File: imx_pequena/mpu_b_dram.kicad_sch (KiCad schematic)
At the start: 19 parts, among them U1 MCIMX6Z0DVM09AB, U2 MT41K64M16TW-107:J_TR

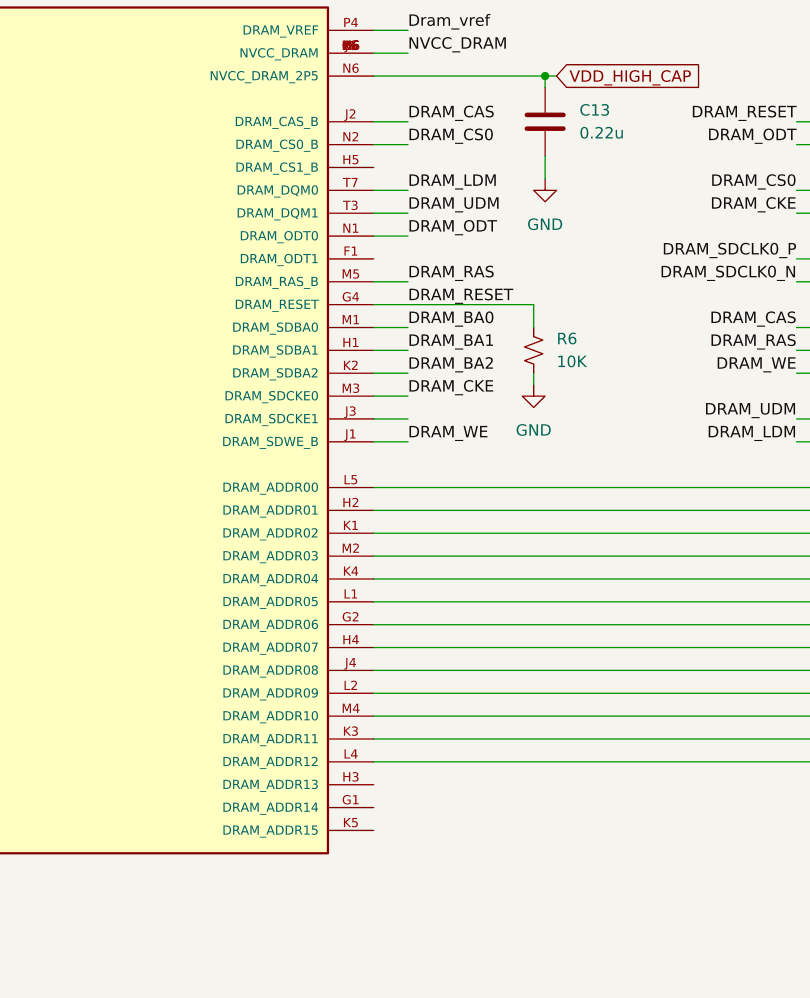
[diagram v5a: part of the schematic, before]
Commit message: Pinout updates
Updated pinout files, changed pinout of gpio 1 and 3
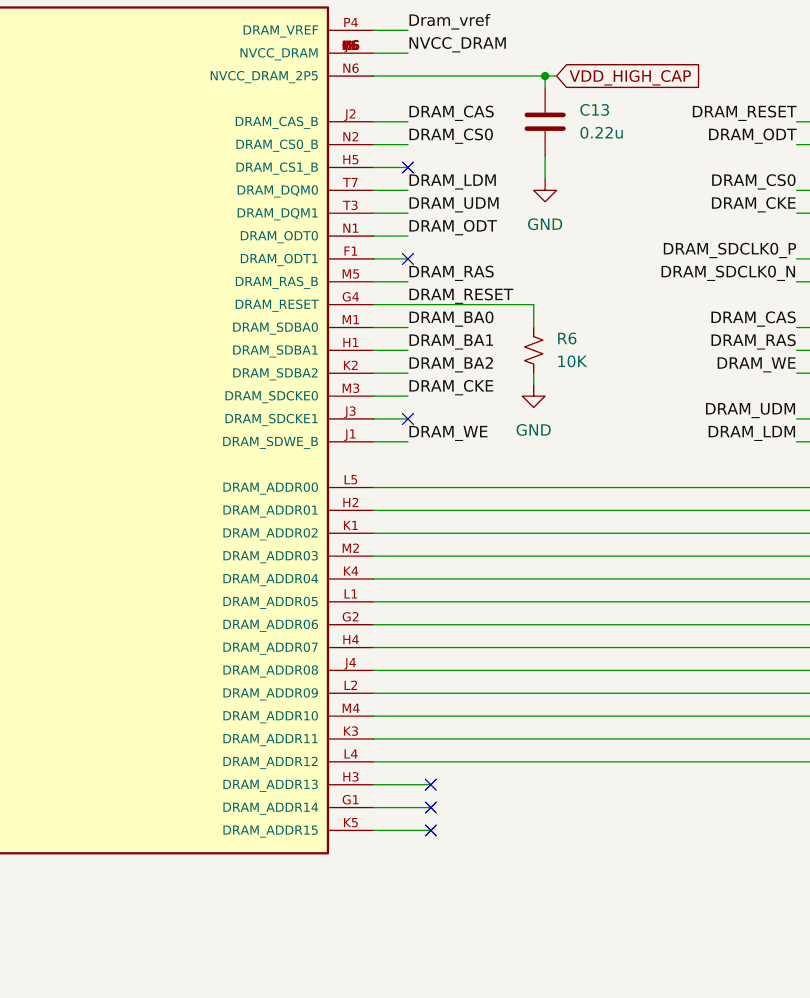
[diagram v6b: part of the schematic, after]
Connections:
- no-connect marks 0 -> 6
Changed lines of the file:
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@@
   (junction (at 76.2 181.61) (diameter 0) (color 0 0 0 0)
   )
+  (no_connect (at 124.46 63.5))
+  (no_connect (at 124.46 53.34))
+  (no_connect (at 124.46 81.28))
+  (no_connect (at 127 121.92))
+  (no_connect (at 127 124.46))
+  (no_connect (at 127 127))
   (bus_entry (at 255.27 88.9) (size -2.54 2.54)
     (stroke (width 0) (type default) (color 0 0 0 0))
@@
     (stroke (width 0) (type default) (color 0 0 0 0))
   )
+  (wire (pts (xy 120.65 63.5) (xy 124.46 63.5))
+    (stroke (width 0) (type default) (color 0 0 0 0))
+  )
   (wire (pts (xy 52.07 119.38) (xy 59.69 119.38))
     (stroke (width 0) (type default) (color 0 0 0 0))
@@
     (stroke (width 0) (type default) (color 0 0 0 0))
   )
+  (wire (pts (xy 120.65 121.92) (xy 127 121.92))
+    (stroke (width 0) (type default) (color 0 0 0 0))
+  )
   (wire (pts (xy 52.07 127) (xy 59.69 127))
     (stroke (width 0) (type default) (color 0 0 0 0))
@@
     (stroke (width 0) (type default) (color 0 0 0 0))
   )
+  (wire (pts (xy 120.65 124.46) (xy 127 124.46))
+    (stroke (width 0) (type default) (color 0 0 0 0))
+  )
   (wire (pts (xy 276.86 24.13) (xy 276.86 22.86))
     (stroke (width 0) (type default) (color 0 0 0 0))
@@
     (stroke (width 0) (type default) (color 0 0 0 0))
   )
+  (wire (pts (xy 120.65 53.34) (xy 124.46 53.34))
+    (stroke (width 0) (type default) (color 0 0 0 0))
+  )
   (wire (pts (xy 139.7 52.07) (xy 139.7 54.61))
     (stroke (width 0) (type default) (color 0 0 0 0))
@@
     (stroke (width 0) (type default) (color 0 0 0 0))
   )
+  (wire (pts (xy 120.65 127) (xy 127 127))
+    (stroke (width 0) (type default) (color 0 0 0 0))
+  )

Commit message: Part Assignment
Assigned GPIOs and assigned footprints to most parts
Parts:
- C10, C11, C12, C13, C14, C15, C16, C17, C8, C9: footprint (none) -> Capacitor_SMD:C_0402_1005Metric
- C7: footprint (none) -> Capacitor_SMD:C_0603_1608Metric
- R3, R4, R5, R6, R7, R8: footprint (none) -> Resistor_SMD:R_0402_1005Metric
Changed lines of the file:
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@@
       (effects (font (size 1.27 1.27)) (justify left))
     )
-    (property "Footprint" "" (id 2) (at 277.8252 38.1 0)
+    (property "Footprint" "Capacitor_SMD:C_0402_1005Metric" (id 2) (at 277.8252 38.1 0)
       (effects (font (size 1.27 1.27)) hide)
     )
@@
       (effects (font (size 1.27 1.27)) (justify left))
     )
-    (property "Footprint" "" (id 2) (at 140.6652 52.07 0)
+    (property "Footprint" "Capacitor_SMD:C_0402_1005Metric" (id 2) (at 140.6652 52.07 0)
       (effects (font (size 1.27 1.27)) hide)
     )
@@
       (effects (font (size 1.27 1.27)) (justify left))
     )
-    (property "Footprint" "" (id 2) (at 276.86 20.32 0)
+    (property "Footprint" "Resistor_SMD:R_0402_1005Metric" (id 2) (at 276.86 20.32 0)
       (effects (font (size 1.27 1.27)) hide)
     )
@@
       (effects (font (size 1.27 1.27)) (justify left))
     )
-    (property "Footprint" "" (id 2) (at 138.43 73.66 0)
+    (property "Footprint" "Resistor_SMD:R_0402_1005Metric" (id 2) (at 138.43 73.66 0)
       (effects (font (size 1.27 1.27)) hide)
     )
@@
       (effects (font (size 1.27 1.27)) (justify right))
     )
-    (property "Footprint" "" (id 2) (at 48.26 185.42 0)
+    (property "Footprint" "Resistor_SMD:R_0402_1005Metric" (id 2) (at 48.26 185.42 0)
       (effects (font (size 1.27 1.27)) hide)
     )
@@
       (effects (font (size 1.27 1.27)) (justify left))
     )
-    (property "Footprint" "" (id 2) (at 83.5152 190.5 0)
+    (property "Footprint" "Capacitor_SMD:C_0402_1005Metric" (id 2) (at 83.5152 190.5 0)
       (effects (font (size 1.27 1.27)) hide)
     )
@@
       (effects (font (size 1.27 1.27)) (justify left))
     )
-    (property "Footprint" "" (id 2) (at 56.8452 175.26 0)
+    (property "Footprint" "Capacitor_SMD:C_0402_1005Metric" (id 2) (at 56.8452 175.26 0)
       (effects (font (size 1.27 1.27)) hide)
     )
@@
       (effects (font (size 1.27 1.27)) (justify left))
     )
-    (property "Footprint" "" (id 2) (at 56.8452 189.23 0)
+    (property "Footprint" "Capacitor_SMD:C_0402_1005Metric" (id 2) (at 56.8452 189.23 0)
       (effects (font (size 1.27 1.27)) hide)
     )
@@
       (effects (font (size 1.27 1.27)) (justify left))
     )
-    (property "Footprint" "" (id 2) (at 271.4752 38.1 0)
+    (property "Footprint" "Capacitor_SMD:C_0402_1005Metric" (id 2) (at 271.4752 38.1 0)
       (effects (font (size 1.27 1.27)) hide)
     )
@@
       (effects (font (size 1.27 1.27)) (justify left))
     )
-    (property "Footprint" "" (id 2) (at 232.41 52.07 0)
+    (property "Footprint" "Resistor_SMD:R_0402_1005Metric" (id 2) (at 232.41 52.07 0)
       (effects (font (size 1.27 1.27)) hide)
     )
@@
       (effects (font (size 1.27 1.27)) (justify left))
     )
-    (property "Footprint" "" (id 2) (at 35.2552 181.61 0)
+    (property "Footprint" "Capacitor_SMD:C_0603_1608Metric" (id 2) (at 35.2552 181.61 0)
       (effects (font (size 1.27 1.27)) hide)
     )
@@
       (effects (font (size 1.27 1.27)) (justify left))
     )
-    (property "Footprint" "" (id 2) (at 69.5452 190.5 0)
+    (property "Footprint" "Capacitor_SMD:C_0402_1005Metric" (id 2) (at 69.5452 190.5 0)
       (effects (font (size 1.27 1.27)) hide)
     )
@@
       (effects (font (size 1.27 1.27)) (justify right))
     )
-    (property "Footprint" "" (id 2) (at 48.26 171.45 0)
+    (property "Footprint" "Resistor_SMD:R_0402_1005Metric" (id 2) (at 48.26 171.45 0)
       (effects (font (size 1.27 1.27)) hide)
     )
@@
       (effects (font (size 1.27 1.27)) (justify left))
     )
-    (property "Footprint" "" (id 2) (at 53.34 74.93 0)
+    (property "Footprint" "Resistor_SMD:R_0402_1005Metric" (id 2) (at 53.34 74.93 0)
       (effects (font (size 1.27 1.27)) hide)
     )
@@
       (effects (font (size 1.27 1.27)) (justify left))
     )
-    (property "Footprint" "" (id 2) (at 271.4752 53.34 0)
+    (property "Footprint" "Capacitor_SMD:C_0402_1005Metric" (id 2) (at 271.4752 53.34 0)
       (effects (font (size 1.27 1.27)) hide)
     )
@@
       (effects (font (size 1.27 1.27)) (justify left))
     )
-    (property "Footprint" "" (id 2) (at 77.1652 190.5 0)
+    (property "Footprint" "Capacitor_SMD:C_0402_1005Metric" (id 2) (at 77.1652 190.5 0)
       (effects (font (size 1.27 1.27)) hide)
     )
@@
       (effects (font (size 1.27 1.27)) (justify left))
     )
-    (property "Footprint" "" (id 2) (at 277.8252 53.34 0)
-      (effects (font (size 1.27 1.27)) hide)
-    )
+    (property "Footprint" "Capacitor_SMD:C_0402_1005Metric" (id 2) (at 277.8252 53.34 0)
+      (effects (font (size 1.27 1.27)) hide)
+    )
